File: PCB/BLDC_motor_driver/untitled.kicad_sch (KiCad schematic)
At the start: 12 parts, among them Q8 CSD18533Q5A, Q9 CSD18533Q5A, U3 IR2104, U9 INA240A1D

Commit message: pcb progress
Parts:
- removed C3: C_Polarized, symbol Device:C_Polarized
- added U1: INA240A2D, Package_SO:SOIC-8_3.9x4.9mm_P1.27mm, symbol Amplifier_Current:INA240A2D
- added U4: INA240A3D, Package_SO:SOIC-8_3.9x4.9mm_P1.27mm, symbol Amplifier_Current:INA240A3D
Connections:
- net GND: now also R3.2, U9.1 (-), U9.2 (GND), U9.4 (GND); no longer C2.2, Q8.1 (S), Q8.2 (S), Q8.3 (S), U3.4 (COM)
- net PWR_3.3V: now also U9.6 (V+)
- net VISENSE_A: now also R4.2
- net at U9.5: now also R4.1
- net at R3.1, U9.8 (+): now also C2.2, Q8.1 (S), Q8.2 (S), Q8.3 (S), U3.4 (COM)
- new net: U1.2 (GND), U1.4 (GND)
- new net: U4.2 (GND), U4.4 (GND)
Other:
- moved on the sheet: R3, R4, U9

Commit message: more pcb progress
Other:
- moved on the sheet: D1
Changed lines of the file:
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@@
 	)
 	(junction
-		(at 96.52 54.61)
+		(at 96.52 57.15)
 		(diameter 0)
 		(color 0 0 0 0)
@@
 	(wire
 		(pts
-			(xy 96.52 43.18) (xy 96.52 54.61)
+			(xy 96.52 49.53) (xy 96.52 57.15)
 		)
 		(stroke
@@
 	(wire
 		(pts
-			(xy 157.48 54.61) (xy 157.48 63.5)
+			(xy 157.48 57.15) (xy 157.48 63.5)
 		)
 		(stroke
@@
 	(wire
 		(pts
-			(xy 109.22 54.61) (xy 157.48 54.61)
+			(xy 127 57.15) (xy 157.48 57.15)
 		)
 		(stroke
@@
 	(wire
 		(pts
-			(xy 86.36 43.18) (xy 96.52 43.18)
+			(xy 88.9 49.53) (xy 96.52 49.53)
 		)
 		(stroke
@@
 	(wire
 		(pts
-			(xy 157.48 115.57) (xy 157.48 121.92)
+			(xy 157.48 115.57) (xy 157.48 119.38)
 		)
 		(stroke
@@
 	(wire
 		(pts
-			(xy 182.88 121.92) (xy 182.88 116.84)
+			(xy 182.88 119.38) (xy 182.88 116.84)
 		)
 		(stroke
@@
 	(wire
 		(pts
-			(xy 96.52 54.61) (xy 101.6 54.61)
+			(xy 96.52 57.15) (xy 119.38 57.15)
 		)
 		(stroke
@@
 	(wire
 		(pts
-			(xy 96.52 54.61) (xy 96.52 60.96)
+			(xy 96.52 57.15) (xy 96.52 60.96)
 		)
 		(stroke
@@
 	(wire
 		(pts
-			(xy 80.01 83.82) (xy 80.01 54.61)
-		)
-		(stroke
-			(width 0)
-			(type default)
-		)
-	)
-	(wire
-		(pts
-			(xy 80.01 54.61) (xy 96.52 54.61)
+			(xy 80.01 83.82) (xy 80.01 57.15)
+		)
+		(stroke
+			(width 0)
+			(type default)
+		)
+	)
+	(wire
+		(pts
+			(xy 80.01 57.15) (xy 96.52 57.15)
 		)
 		(stroke
@@
 	(hierarchical_label "PWR_12V"
 		(shape input)
-		(at 86.36 43.18 180)
+		(at 88.9 49.53 180)
 		(effects
 			(font
@@
 	(symbol
 		(lib_id "Device:D_Filled")
-		(at 105.41 54.61 180)
+		(at 123.19 57.15 180)
 		(unit 1)
 		(exclude_from_sim no)
@@
 		(fields_autoplaced yes)
 		(property "Reference" "D1"
-			(at 105.41 48.26 0)
+			(at 123.19 50.8 0)
 			(effects
 				(font
@@
 		)
 		(property "Value" "D_Filled"
-			(at 105.41 50.8 0)
+			(at 123.19 53.34 0)
 			(effects
 				(font
@@
 		)
 		(property "Footprint" ""
-			(at 105.41 54.61 0)
+			(at 123.19 57.15 0)
 			(effects
 				(font
@@
 		)
 		(property "Datasheet" "~"
-			(at 105.41 54.61 0)
+			(at 123.19 57.15 0)
 			(effects
 				(font
@@
 		)
 		(property "Description" "Diode, filled shape"
-			(at 105.41 54.61 0)
+			(at 123.19 57.15 0)
 			(effects
 				(font
@@
 		)
 		(property "Sim.Device" "D"
-			(at 105.41 54.61 0)
+			(at 123.19 57.15 0)
 			(effects
 				(font
@@
 		)
 		(property "Sim.Pins" "1=K 2=A"
-			(at 105.41 54.61 0)
+			(at 123.19 57.15 0)
 			(effects
 				(font
@@
 	(symbol
 		(lib_id "power:GND")
-		(at 182.88 121.92 0)
+		(at 182.88 119.38 0)
 		(unit 1)
 		(exclude_from_sim no)
@@
 		(on_board yes)
 		(dnp no)
-		(fields_autoplaced yes)
 		(property "Reference" "#PWR03"
-			(at 182.88 128.27 0)
+			(at 182.88 125.73 0)
 			(effects
 				(font
@@
 		)
 		(property "Value" "GND"
-			(at 182.88 127 0)
+			(at 182.88 123.444 0)
 			(effects
 				(font
@@
 		)
 		(property "Footprint" ""
-			(at 182.88 121.92 0)
+			(at 182.88 119.38 0)
 			(effects
 				(font
@@
 		)
 		(property "Datasheet" ""
-			(at 182.88 121.92 0)
+			(at 182.88 119.38 0)
 			(effects
 				(font
@@
 		)
 		(property "Description" "Power symbol creates a global label with name \"GND\" , ground"
-			(at 182.88 121.92 0)
+			(at 182.88 119.38 0)
 			(effects
 				(font
@@
 	(symbol
 		(lib_id "power:GND")
-		(at 157.48 121.92 0)
+		(at 157.48 119.38 0)
 		(unit 1)
 		(exclude_from_sim no)
@@
 		(on_board yes)
 		(dnp no)
-		(fields_autoplaced yes)
 		(property "Reference" "#PWR02"
-			(at 157.48 128.27 0)
+			(at 157.48 125.73 0)
 			(effects
 				(font
@@
 		)
 		(property "Value" "GND"
-			(at 157.48 127 0)
+			(at 157.48 123.444 0)
 			(effects
 				(font
@@
 		)
 		(property "Footprint" ""
-			(at 157.48 121.92 0)
+			(at 157.48 119.38 0)
 			(effects
 				(font
@@
 		)
 		(property "Datasheet" ""
-			(at 157.48 121.92 0)
+			(at 157.48 119.38 0)
 			(effects
 				(font
@@
 		)
 		(property "Description" "Power symbol creates a global label with name \"GND\" , ground"
-			(at 157.48 121.92 0)
-			(effects
-				(font
+			(at 157.48 119.38 0)
+			(effects
+				(font

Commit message: more progress
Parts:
- added C25, C26: 100n, symbol Device:C
- added R10, R9: R, symbol Device:R
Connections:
- net GND: now also U9.7 (REF1), C25.2, R10.1; no longer U9.1 (-)
- net PWR_3.3V: now also U9.3 (REF2), C25.1
- net at C2.2, Q8.1 (S), Q8.2 (S)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: now also R9.1; no longer U9.8 (+)
- new net: C26.2, R10.2, U9.1 (-)
- new net: C26.1, R9.2, U9.8 (+)
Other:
- moved on the sheet: C1, R4, U9

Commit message: further PCB progress
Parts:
- added J5: PHASE_A, TerminalBlock_MetzConnect:TerminalBlock_MetzConnect_360410_1x01_Horizontal_ScrewM3.0, symbol Connector:Screw_Terminal_01x01
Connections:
- net PHASE A: no longer names the net of C1.2, Q8.5 (D), Q9.1 (S), Q9.2 (S), Q9.3 (S), U3.6 (VS)
- net PHASE A: now also J5.1 (Pin_1)
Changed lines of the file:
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@@
-		)
-	)
-	(hierarchical_label "PHASE A"
-		(shape input)
-		(at 168.91 78.74 0)
-		(effects
-			(font
-				(size 1.27 1.27)
-			)
-			(justify left)
 		)
 	)
@@
 					(unit 1)
 				)
+			)
+		)
+	)
+	(symbol
+		(lib_id "Connector:Screw_Terminal_01x01")
+		(at 173.99 78.74 0)
+		(unit 1)
+		(exclude_from_sim no)
+		(in_bom yes)
+		(on_board yes)
+		(dnp no)
+		(fields_autoplaced yes)
+		(property "Reference" "J5"
+			(at 176.53 77.4699 0)
+			(effects
+				(font
+					(size 1.27 1.27)
+				)
+				(justify left)
+			)
+		)
+		(property "Value" "PHASE_A"
+			(at 176.53 80.0099 0)
+			(effects
+				(font
+					(size 1.27 1.27)
+				)
+				(justify left)
+			)
+		)
+		(property "Footprint" "TerminalBlock_MetzConnect:TerminalBlock_MetzConnect_360410_1x01_Horizontal_ScrewM3.0"
+			(at 173.99 78.74 0)
+			(effects
+				(font
+					(size 1.27 1.27)
+				)
+				(hide yes)
+			)
+		)
+		(property "Datasheet" "~"
+			(at 173.99 78.74 0)
+			(effects
+				(font
+					(size 1.27 1.27)
+				)
+				(hide yes)
+			)
+		)
+		(property "Description" "Generic screw terminal, single row, 01x01, script generated (kicad-library-utils/schlib/autogen/connector/)"
+			(at 173.99 78.74 0)
+			(effects
+				(font
+					(size 1.27 1.27)
+				)
+				(hide yes)
+			)
+		)
+		(pin "1"
+		)
+		(instances
+			(project ""
+				(path "/1217eed8-ee8e-4ad2-9f65-aaa3eab4838e/aab35023-a3fe-424f-b0db-c44ab5049a21"
+					(reference "J5")
+					(unit 1)
+				)

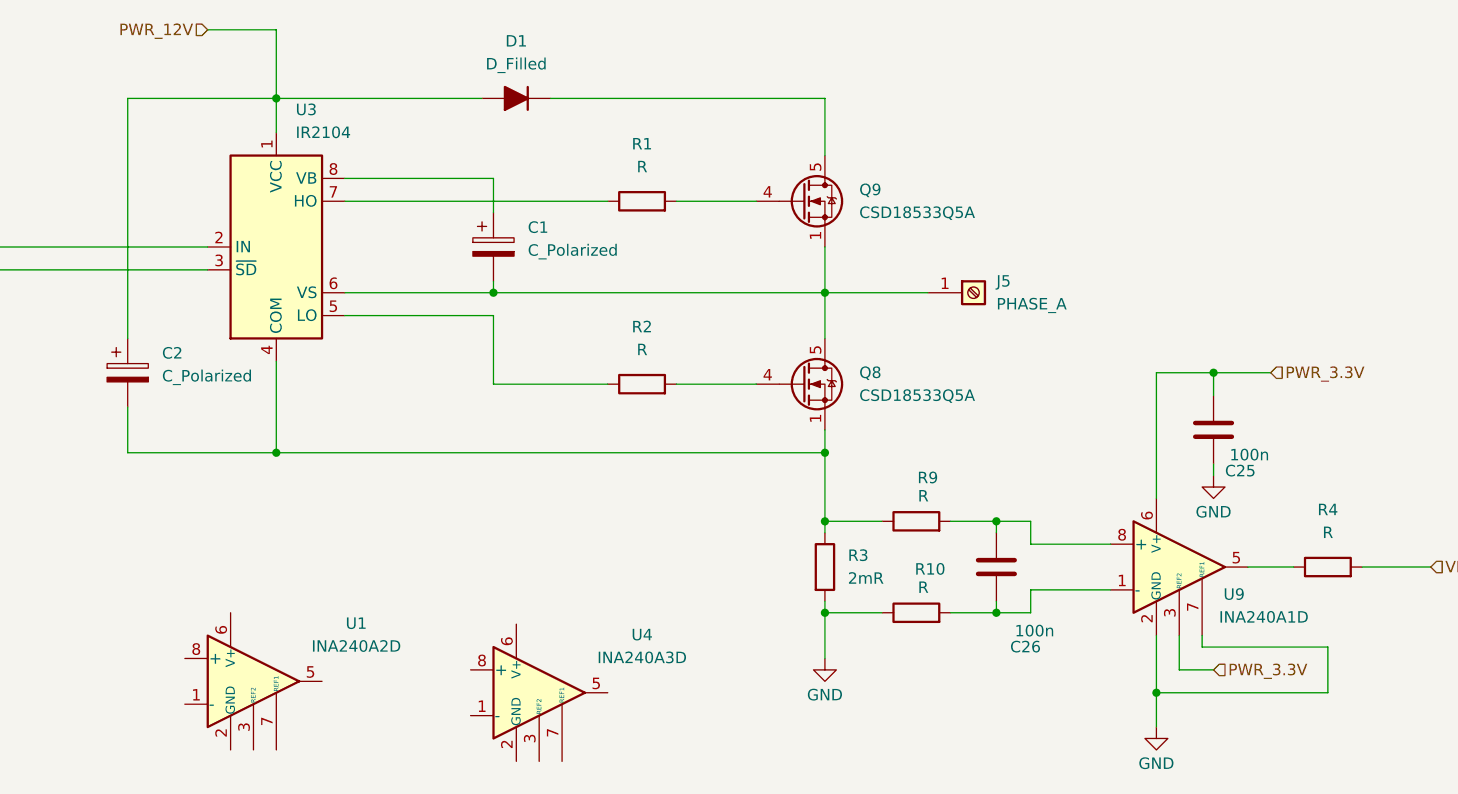
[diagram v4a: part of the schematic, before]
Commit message: PCB schematic progress - footprints and values
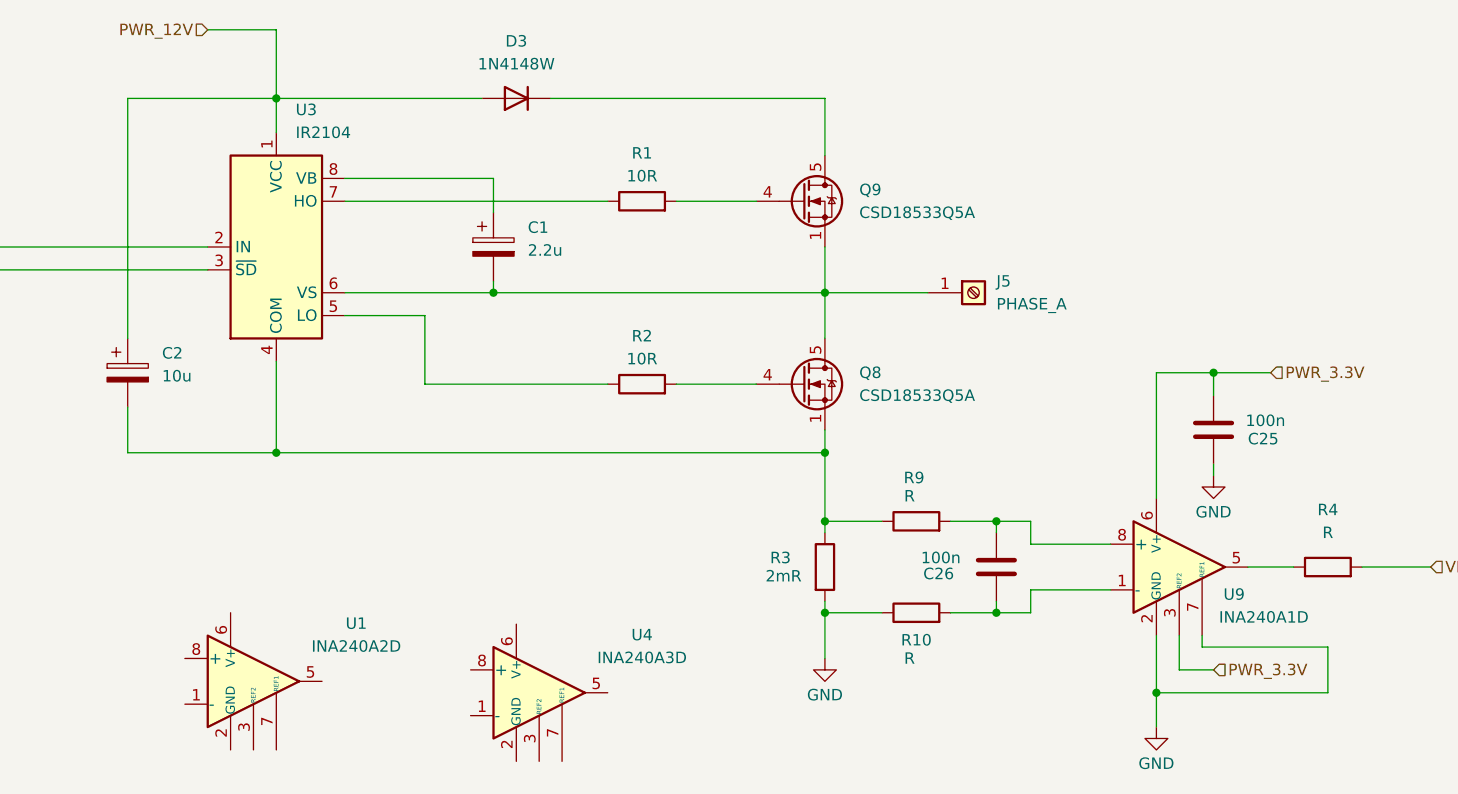
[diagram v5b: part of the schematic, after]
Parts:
- removed D1: D_Filled, symbol Device:D_Filled
- added D3: 1N4148W, Diode_SMD:D_SOD-123, symbol Diode:1N4148W
- C1: value C_Polarized -> 2.2u; footprint (none) -> Capacitor_Tantalum_SMD:CP_EIA-2012-15_AVX-P
- C2: value C_Polarized -> 10u; footprint (none) -> Capacitor_Tantalum_SMD:CP_EIA-2012-12_Kemet-R
- C25, C26: footprint (none) -> Capacitor_SMD:C_0402_1005Metric
- R1, R2: value R -> 10R; footprint (none) -> Resistor_SMD:R_0603_1608Metric
- R3: footprint (none) -> Resistor_SMD:R_2512_6332Metric
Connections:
- net PWR_12V: now also D3.2 (A)
- net at Q9.5 (D): now also D3.1 (K)
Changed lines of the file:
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@@
 	(wire
 		(pts
-			(xy 120.65 88.9) (xy 133.35 88.9)
+			(xy 113.03 88.9) (xy 133.35 88.9)
 		)
 		(stroke
@@
 	(wire
 		(pts
-			(xy 120.65 81.28) (xy 104.14 81.28)
+			(xy 113.03 81.28) (xy 104.14 81.28)
 		)
 		(stroke
@@
 	(wire
 		(pts
-			(xy 120.65 88.9) (xy 120.65 81.28)
+			(xy 113.03 88.9) (xy 113.03 81.28)
 		)
 		(stroke
@@
 			)
 			(justify left)
-		)
-	)
-	(symbol
-		(lib_id "Device:D_Filled")
-		(at 123.19 57.15 180)
-		(unit 1)
-		(exclude_from_sim no)
-		(in_bom yes)
-		(on_board yes)
-		(dnp no)
-		(fields_autoplaced yes)
-		(property "Reference" "D1"
-			(at 123.19 50.8 0)
-			(effects
-				(font
-					(size 1.27 1.27)
-				)
-			)
-		)
-		(property "Value" "D_Filled"
-			(at 123.19 53.34 0)
-			(effects
-				(font
-					(size 1.27 1.27)
-				)
-			)
-		)
-		(property "Footprint" ""
-			(at 123.19 57.15 0)
-			(effects
-				(font
-					(size 1.27 1.27)
-				)
-				(hide yes)
-			)
-		)
-		(property "Datasheet" "~"
-			(at 123.19 57.15 0)
-			(effects
-				(font
-					(size 1.27 1.27)
-				)
-				(hide yes)
-			)
-		)
-		(property "Description" "Diode, filled shape"
-			(at 123.19 57.15 0)
-			(effects
-				(font
-					(size 1.27 1.27)
-				)
-				(hide yes)
-			)
-		)
-		(property "Sim.Device" "D"
-			(at 123.19 57.15 0)
-			(effects
-				(font
-					(size 1.27 1.27)
-				)
-				(hide yes)
-			)
-		)
-		(property "Sim.Pins" "1=K 2=A"
-			(at 123.19 57.15 0)
-			(effects
-				(font
-					(size 1.27 1.27)
-				)
-				(hide yes)
-			)
-		)
-		(pin "1"
-		)
-		(pin "2"
-		)
-		(instances
-			(project ""
-				(path "/1217eed8-ee8e-4ad2-9f65-aaa3eab4838e/aab35023-a3fe-424f-b0db-c44ab5049a21"
-					(reference "D1")
-					(unit 1)
-				)
-			)
 		)
 	)
@@
 		(dnp no)
 		(property "Reference" "R10"
-			(at 169.164 109.474 90)
+			(at 167.64 117.348 90)
 			(effects
 				(font
@@
 		)
 		(property "Value" "R"
-			(at 168.402 111.506 90)
+			(at 166.878 119.38 90)
 			(effects
 				(font
@@
 		(on_board yes)
 		(dnp no)
-		(fields_autoplaced yes)
 		(property "Reference" "R3"
-			(at 160.02 107.9499 0)
+			(at 151.384 108.204 0)
 			(effects
 				(font
@@
 		)
 		(property "Value" "2mR"
-			(at 160.02 110.4899 0)
-			(effects
-				(font
-					(size 1.27 1.27)
-				)
-				(justify left)
-			)
-		)
-		(property "Footprint" ""
+			(at 150.876 110.236 0)
+			(effects
+				(font
+					(size 1.27 1.27)
+				)
+				(justify left)
+			)
+		)
+		(property "Footprint" "Resistor_SMD:R_2512_6332Metric"
 			(at 155.702 109.22 90)
 			(effects
@@
 			)
 		)
-		(property "Datasheet" "~"
+		(property "Datasheet" "https://www.tme.eu/en/details/mpr251205fr002/smd-resistors/wayon/"
 			(at 157.48 109.22 0)
 			(effects
@@
 			)
 		)
-		(property "Value" "C_Polarized"
+		(property "Value" "10u"
 			(at 83.82 88.0109 0)
 			(effects
@@
 			)
 		)
-		(property "Footprint" ""
+		(property "Footprint" "Capacitor_Tantalum_SMD:CP_EIA-2012-12_Kemet-R"
 			(at 80.9752 91.44 0)
 			(effects
@@
 			)
 		)
-		(property "Value" "C_Polarized"
+		(property "Value" "2.2u"
 			(at 124.46 74.0409 0)
 			(effects
@@
 			)
 		)
-		(property "Footprint" ""
+		(property "Footprint" "Capacitor_Tantalum_SMD:CP_EIA-2012-15_AVX-P"
 			(at 121.6152 77.47 0)
 			(effects
@@
 				(path "/1217eed8-ee8e-4ad2-9f65-aaa3eab4838e/aab35023-a3fe-424f-b0db-c44ab5049a21"
 					(reference "C1")
+					(unit 1)
+				)
+			)
+		)
+	)
+	(symbol
+		(lib_id "Diode:1N4148W")
+		(at 123.19 57.15 180)
+		(unit 1)
+		(exclude_from_sim no)
+		(in_bom yes)
+		(on_board yes)
+		(dnp no)
+		(fields_autoplaced yes)
+		(property "Reference" "D3"
+			(at 123.19 50.8 0)
+			(effects
+				(font
+					(size 1.27 1.27)
+				)
+			)
+		)
+		(property "Value" "1N4148W"
+			(at 123.19 53.34 0)
+			(effects
+				(font
+					(size 1.27 1.27)
+				)
+			)
+		)
+		(property "Footprint" "Diode_SMD:D_SOD-123"
+			(at 123.19 52.705 0)
+			(effects
+				(font
+					(size 1.27 1.27)
+				)
+				(hide yes)
+			)
+		)
+		(property "Datasheet" "https://www.vishay.com/docs/85748/1n4148w.pdf"
+			(at 123.19 57.15 0)
+			(effects
+				(font
+					(size 1.27 1.27)
+				)
+				(hide yes)
+			)
+		)
+		(property "Description" "75V 0.15A Fast Switching Diode, SOD-123"
+			(at 123.19 57.15 0)
+			(effects
+				(font
+					(size 1.27 1.27)
+				)
+				(hide yes)
+			)
+		)
+		(property "Sim.Device" "D"
+			(at 123.19 57.15 0)
+			(effects
+				(font
+					(size 1.27 1.27)
+				)
+				(hide yes)
+			)
+		)
+		(property "Sim.Pins" "1=K 2=A"
+			(at 123.19 57.15 0)
+			(effects
+				(font
+					(size 1.27 1.27)
+				)
+				(hide yes)
+			)
+		)
+		(pin "1"
+		)
+		(pin "2"
+		)
+		(instances
+			(project ""
+				(path "/1217eed8-ee8e-4ad2-9f65-aaa3eab4838e/aab35023-a3fe-424f-b0db-c44ab5049a21"
+					(reference "D3")
 					(unit 1)
 				)
@@
 		(dnp no)
 		(property "Reference" "R9"
-			(at 168.91 99.314 90)
+			(at 167.386 99.314 90)
 			(effects
 				(font
@@
 		)
 		(property "Value" "R"
-			(at 168.402 101.346 90)
+			(at 166.878 101.346 90)
 			(effects
 				(font
@@
 		(dnp no)
 		(property "Reference" "C26"
-			(at 178.054 118.11 0)
+			(at 168.402 109.982 0)
 			(effects
 				(font
@@
 		)
 		(property "Value" "100n"
-			(at 178.562 116.332 0)
-			(effects
-				(font
-					(size 1.27 1.27)
-				)
-				(justify left)
-			)
-		)
-		(property "Footprint" ""
+			(at 168.148 108.204 0)
+			(effects
+				(font
+					(size 1.27 1.27)
+				)
+				(justify left)
+			)
+		)
+		(property "Footprint" "Capacitor_SMD:C_0402_1005Metric"
 			(at 177.4952 113.03 0)
 			(effects
@@
 		(dnp no)
 		(property "Reference" "C25"
-			(at 201.93 98.552 0)
+			(at 204.47 94.996 0)
 			(effects
 				(font
@@
 		)
 		(property "Value" "100n"
-			(at 202.438 96.774 0)
-			(effects
-				(font
-					(size 1.27 1.27)
-				)
-				(justify left)
-			)
-		)
-		(property "Footprint" ""
+			(at 204.216 92.964 0)
+			(effects
+				(font
+					(size 1.27 1.27)
+				)
+				(justify left)
+			)
+		)
+		(property "Footprint" "Capacitor_SMD:C_0402_1005Metric"
 			(at 201.6252 97.79 0)
 			(effects
@@
 		(on_board yes)
 		(dnp no)
-		(fields_autoplaced yes)
 		(property "Reference" "R2"
-			(at 137.16 82.55 90)
-			(effects
-				(font
-					(size 1.27 1.27)
-				)
-			)
-		)
-		(property "Value" "R"
-			(at 137.16 85.09 90)
-			(effects
-				(font
-					(size 1.27 1.27)
-				)
-			)
-		)
-		(property "Footprint" ""
+			(at 137.16 83.566 90)
+			(effects
+				(font
+					(size 1.27 1.27)
+				)
+			)
+		)
+		(property "Value" "10R"
+			(at 137.16 86.106 90)
+			(effects
+				(font
+					(size 1.27 1.27)
+				)
+			)
+		)
+		(property "Footprint" "Resistor_SMD:R_0603_1608Metric"
 			(at 137.16 90.678 90)
 			(effects
@@
 		(on_board yes)
 		(dnp no)
-		(fields_autoplaced yes)
 		(property "Reference" "R1"
-			(at 137.16 62.23 90)
-			(effects
-				(font
-					(size 1.27 1.27)
-				)
-			)
-		)
-		(property "Value" "R"
-			(at 137.16 64.77 90)
-			(effects
-				(font
-					(size 1.27 1.27)
-				)
-			)
-		)
-		(property "Footprint" ""
+			(at 137.16 63.246 90)
+			(effects
+				(font
+					(size 1.27 1.27)
+				)
+			)
+		)
+		(property "Value" "10R"
+			(at 137.16 65.786 90)
+			(effects
+				(font
+					(size 1.27 1.27)
+				)
+			)
+		)
+		(property "Footprint" "Resistor_SMD:R_0603_1608Metric"
 			(at 137.16 70.358 90)
 			(effects

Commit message: PCB v2 progress...
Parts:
- removed J5: PHASE_A, TerminalBlock_MetzConnect:TerminalBlock_MetzConnect_360410_1x01_Horizontal_ScrewM3.0, symbol Connector:Screw_Terminal_01x01
- removed R4: R, symbol Device:R
- removed U4: INA240A3D, Package_SO:SOIC-8_3.9x4.9mm_P1.27mm, symbol Amplifier_Current:INA240A3D
- removed U9: INA240A1D, Package_SO:SOIC-8_3.9x4.9mm_P1.27mm, symbol Amplifier_Current:INA240A1D
- added C11: 100n, Capacitor_Tantalum_SMD:CP_EIA-2012-12_Kemet-R, symbol Device:C_Polarized
- added D4, D5: 1N4148W, Diode_SMD:D_SOD-123, symbol Diode:1N4148W
- added H7: PHASE A, MountingHole:MountingHole_2.2mm_M2_Pad_TopBottom, symbol Mechanical:MountingHole_Pad
- added R11: 4.7K, Resistor_SMD:R_0603_1608Metric, symbol Device:R
- added U4: LMV393, Package_SO:VSSOP-8_2.3x2mm_P0.5mm, symbol Comparator:LMV393
- C1: footprint Capacitor_Tantalum_SMD:CP_EIA-2012-15_AVX-P -> Capacitor_Tantalum_SMD:CP_EIA-2012-12_Kemet-R
- C2: value 10u -> 470u
- R10: value R -> 510R; footprint (none) -> Resistor_SMD:R_0603_1608Metric
- R9: value R -> 330R; footprint (none) -> Resistor_SMD:R_0603_1608Metric
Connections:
- net SD_A is gone; now on net GND: U3.3 (~{SD})
- net GND: now also C2.2, C26.2, U1.1 (-), U1.2 (GND), U1.3 (REF2), U1.4 (GND), U1.7 (REF1), U3.4 (COM), C11.2, R11.1, U4.1
- net PWR_12V: now also Q9.5 (D), C11.1
- net PWR_3.3V: now also R9.2, U1.6 (V+), R11.2
- net VISENSE_A: now also U1.5, U4.3 (+)
- net at R10.2: now also R9.1, U4.2 (-); no longer C26.2
- net at C26.1: now also Q8.1 (S), Q8.2 (S), Q8.3 (S), R3.1, U1.8 (+); no longer R9.2
- net at R2.1, U3.5 (LO): now also D5.1 (K)
- net PHASE A: now reaches C1.2, Q8.5 (D), Q9.1 (S), Q9.2 (S), Q9.3 (S), U3.6 (VS)
- net PHASE A: now also H7.1
- net at R1.1, U3.7 (HO): now also D4.1 (K)
- net at C1.1, U3.8 (VB): now also D3.1 (K)
- net at Q8.4 (G), R2.2: now also D5.2 (A)
- net at Q9.4 (G), R1.2: now also D4.2 (A)
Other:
- note added: "12V 40A max"
- note added: "G_A2 - 50V/V V_out = G * I * R_snt V_out_a2 = 50 * 0.001 * I V_out_a2_max = 0.05 * 40A V_out_a2_max = 2V"
- note added: "P_res = I_max^2*R P_res = 40^2*0.001R P_res = 1.6W => P_res = 3W"
- moved on the sheet: C1, C2, C25, C26, D3, Q8, Q9, R1, R2, R3, U1, U3

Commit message: Test driver layour finished... final touches
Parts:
- added C30: 100n, Capacitor_SMD:C_0402_1005Metric, symbol Device:C
- added unit 3 of U4
- added unit 2 of U4
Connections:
- net GND: now also C30.2, U4.4 (V-); no longer R11.1, U3.3 (~{SD}), U4.1
- net PWR_3.3V: now also C30.1, U4.8 (V+)
- new net SD_A: R11.1, U3.3 (~{SD}), U4.1
- no-connect marks 0 -> 3
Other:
- moved on the sheet: R10, R11, R9, U4A
